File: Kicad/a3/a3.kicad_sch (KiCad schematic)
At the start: 60 parts, among them J1 Barrel Jack, J2 IDC 34, J3 Conn_02x03_Odd_Even, J4 VGA, J5 AudioJack4, SW1 SW_Push, SW2 SW_SPDT, U1 74HC590A, U10 74HC32, U11 74HC4520, U12 74HC174, U13 MCP100H, U2 74HC590A, U3 SST39SF0x0, U4 62256, U5 W65C02SxP, U6 74HCT540, U7 74HC166, U8 74HCT04, U9 74HC10, Y1 16Mhz

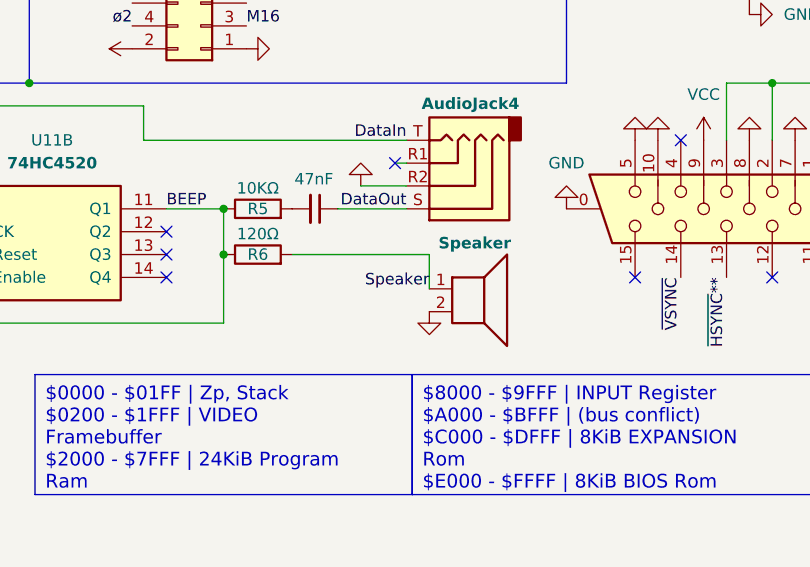
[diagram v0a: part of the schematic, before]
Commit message: Add TTL/MIC level jumper to trs jack
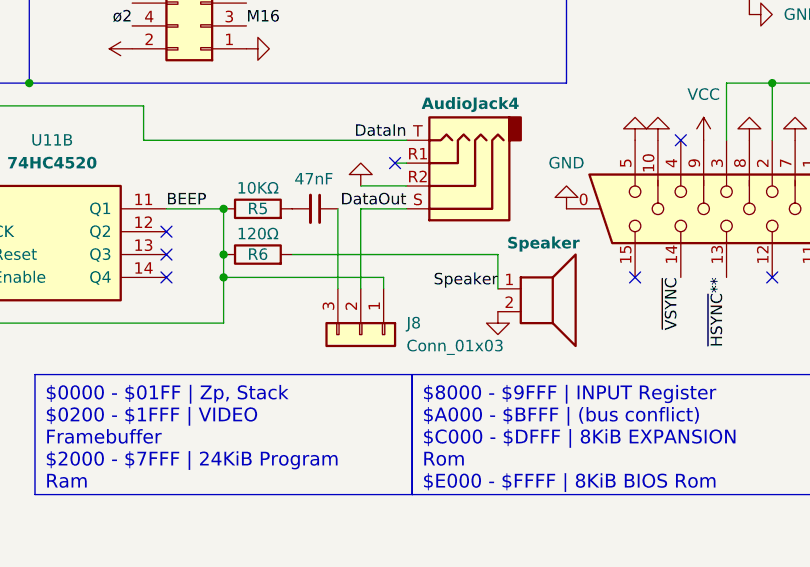
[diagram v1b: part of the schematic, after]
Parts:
- added J8: Conn_01x03, Connector_PinHeader_2.54mm:PinHeader_1x03_P2.54mm_Vertical, symbol Connector_Generic:Conn_01x03
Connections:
- net BEEP: now also J8.1 (Pin_1)
- net DataOut: now also J8.2 (Pin_2); no longer C10.1
- new net: C10.1, J8.3 (Pin_3)
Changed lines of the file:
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@@
 	)
 	(junction
+		(at 207.01 156.21)
+		(diameter 0)
+		(color 0 0 0 0)
+	)
+	(junction
 		(at 185.42 134.62)
 		(diameter 0)
@@
 	(wire
 		(pts
-			(xy 207.01 161.29) (xy 207.01 153.67)
+			(xy 207.01 156.21) (xy 207.01 161.29)
+		)
+		(stroke
+			(width 0)
+			(type default)
+		)
+	)
+	(wire
+		(pts
+			(xy 207.01 153.67) (xy 207.01 156.21)
 		)
 		(stroke
@@
 	(wire
 		(pts
-			(xy 229.87 153.67) (xy 214.63 153.67)
+			(xy 237.49 153.67) (xy 214.63 153.67)
 		)
 		(stroke
@@
 	(wire
 		(pts
+			(xy 222.25 157.48) (xy 222.25 148.59)
+		)
+		(stroke
+			(width 0)
+			(type default)
+		)
+	)
+	(wire
+		(pts
+			(xy 224.79 156.21) (xy 207.01 156.21)
+		)
+		(stroke
+			(width 0)
+			(type default)
+		)
+	)
+	(wire
+		(pts
 			(xy 187.96 110.49) (xy 196.85 110.49)
 		)
@@
 	(wire
 		(pts
-			(xy 219.71 148.59) (xy 227.33 148.59)
-		)
-		(stroke
-			(width 0)
-			(type default)
-		)
-	)
-	(wire
-		(pts
 			(xy 118.11 39.37) (xy 118.11 48.26)
 		)
@@
 		)
 	)
+	(wire
+		(pts
+			(xy 219.71 157.48) (xy 219.71 148.59)
+		)
+		(stroke
+			(width 0)
+			(type default)
+		)
+	)
 	(bus
 		(pts
@@
 	(wire
 		(pts
+			(xy 222.25 148.59) (xy 227.33 148.59)
+		)
+		(stroke
+			(width 0)
+			(type default)
+		)
+	)
+	(wire
+		(pts
 			(xy 102.87 72.39) (xy 106.68 72.39)
 		)
@@
 	(wire
 		(pts
-			(xy 229.87 153.67) (xy 229.87 157.48)
+			(xy 237.49 153.67) (xy 237.49 157.48)
 		)
 		(stroke
@@
 	(wire
 		(pts
+			(xy 224.79 157.48) (xy 224.79 156.21)
+		)
+		(stroke
+			(width 0)
+			(type default)
+		)
+	)
+	(wire
+		(pts
 			(xy 262.89 134.62) (xy 267.97 134.62)
 		)
@@
 	)
 	(label "Speaker"
-		(at 229.87 157.48 180)
+		(at 237.49 157.48 180)
 		(effects
 			(font
@@
 		(lib_name "GND_7")
 		(lib_id "power:GND")
-		(at 229.87 160.02 0)
+		(at 237.49 160.02 0)
 		(unit 1)
 		(exclude_from_sim no)
@@
 		(fields_autoplaced yes)
 		(property "Reference" "#PWR049"
-			(at 229.87 166.37 0)
+			(at 237.49 166.37 0)
 			(effects
 				(font
@@
 		)
 		(property "Value" "GND"
-			(at 229.8701 163.83 90)
+			(at 237.4901 163.83 90)
 			(effects
 				(font
@@
 		)
 		(property "Footprint" ""
-			(at 229.87 160.02 0)
+			(at 237.49 160.02 0)
 			(effects
 				(font
@@
 		)
 		(property "Datasheet" ""
-			(at 229.87 160.02 0)
+			(at 237.49 160.02 0)
 			(effects
 				(font
@@
 		)
 		(property "Description" "Power symbol creates a global label with name \"GND\" , ground"
-			(at 229.87 160.02 0)
+			(at 237.49 160.02 0)
 			(effects
 				(font
@@
 	(symbol
 		(lib_id "Device:Speaker")
-		(at 234.95 157.48 0)
+		(at 242.57 157.48 0)
 		(unit 1)
 		(exclude_from_sim no)
@@
 		(dnp no)
 		(property "Reference" "LS1"
-			(at 239.522 155.956 0)
+			(at 247.142 155.956 0)
 			(effects
 				(font
@@
 		)
 		(property "Value" "Speaker"
-			(at 230.886 152.4 0)
+			(at 238.506 152.4 0)
 			(effects
 				(font
@@
 		)
 		(property "Footprint" "Buzzer_Beeper:MagneticBuzzer_Kingstate_KCG0601"
-			(at 234.95 162.56 0)
+			(at 242.57 162.56 0)
 			(effects
 				(font
@@
 		)
 		(property "Datasheet" "~"
-			(at 234.696 158.75 0)
+			(at 242.316 158.75 0)
 			(effects
 				(font
@@
 		)
 		(property "Description" "Speaker"
-			(at 234.95 157.48 0)
+			(at 242.57 157.48 0)
 			(effects
 				(font
@@
 	)
 	(symbol
+		(lib_id "Connector_Generic:Conn_01x03")
+		(at 222.25 162.56 270)
+		(unit 1)
+		(exclude_from_sim no)
+		(in_bom yes)
+		(on_board yes)
+		(dnp no)
+		(fields_autoplaced yes)
+		(property "Reference" "J8"
+			(at 227.33 161.2899 90)
+			(effects
+				(font
+					(size 1.27 1.27)
+				)
+				(justify left)
+			)
+		)
+		(property "Value" "Conn_01x03"
+			(at 227.33 163.8299 90)
+			(effects
+				(font
+					(size 1.27 1.27)
+				)
+				(justify left)
+			)
+		)
+		(property "Footprint" "Connector_PinHeader_2.54mm:PinHeader_1x03_P2.54mm_Vertical"
+			(at 222.25 162.56 0)
+			(effects
+				(font
+					(size 1.27 1.27)
+				)
+				(hide yes)
+			)
+		)
+		(property "Datasheet" "~"
+			(at 222.25 162.56 0)
+			(effects
+				(font
+					(size 1.27 1.27)
+				)
+				(hide yes)
+			)
+		)
+		(property "Description" "Generic connector, single row, 01x03, script generated (kicad-library-utils/schlib/autogen/connector/)"
+			(at 222.25 162.56 0)
+			(effects
+				(font
+					(size 1.27 1.27)
+				)
+				(hide yes)
+			)
+		)
+		(pin "1"
+		)
+		(pin "2"
+		)
+		(pin "3"
+		)
+		(instances
+			(project ""
+				(path "/fc9f0664-12ec-44ef-b3db-0b33514ae060"
+					(reference "J8")
+					(unit 1)
+				)
+			)
+		)
+	)
+	(symbol
 		(lib_name "GND_1")
 		(lib_id "power:GND")
@@
 		)
 		(instances
-			(project "a2"
+			(project "a3"
 				(path "/fc9f0664-12ec-44ef-b3db-0b33514ae060"
 					(page "2")
